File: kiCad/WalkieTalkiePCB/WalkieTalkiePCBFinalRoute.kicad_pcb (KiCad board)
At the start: 2 copper layers, 55 x 98 mm, 23 parts, among them SW1 UP, SW2 DWN, SW3 MODE, SW4 TLK, SW5 XTRA, U1 BAT-C-10TYPEC_(BMS), U2 PSM-301-Voltage-Regulator, U3 PBS-LED-1606WH-L_(Toggle_Butt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, U4 I2S-128X64-OLED-LCD_, U5 I2S-INMP441_(MIC), U6 Amplifier, U7 ESP-WROOM-32

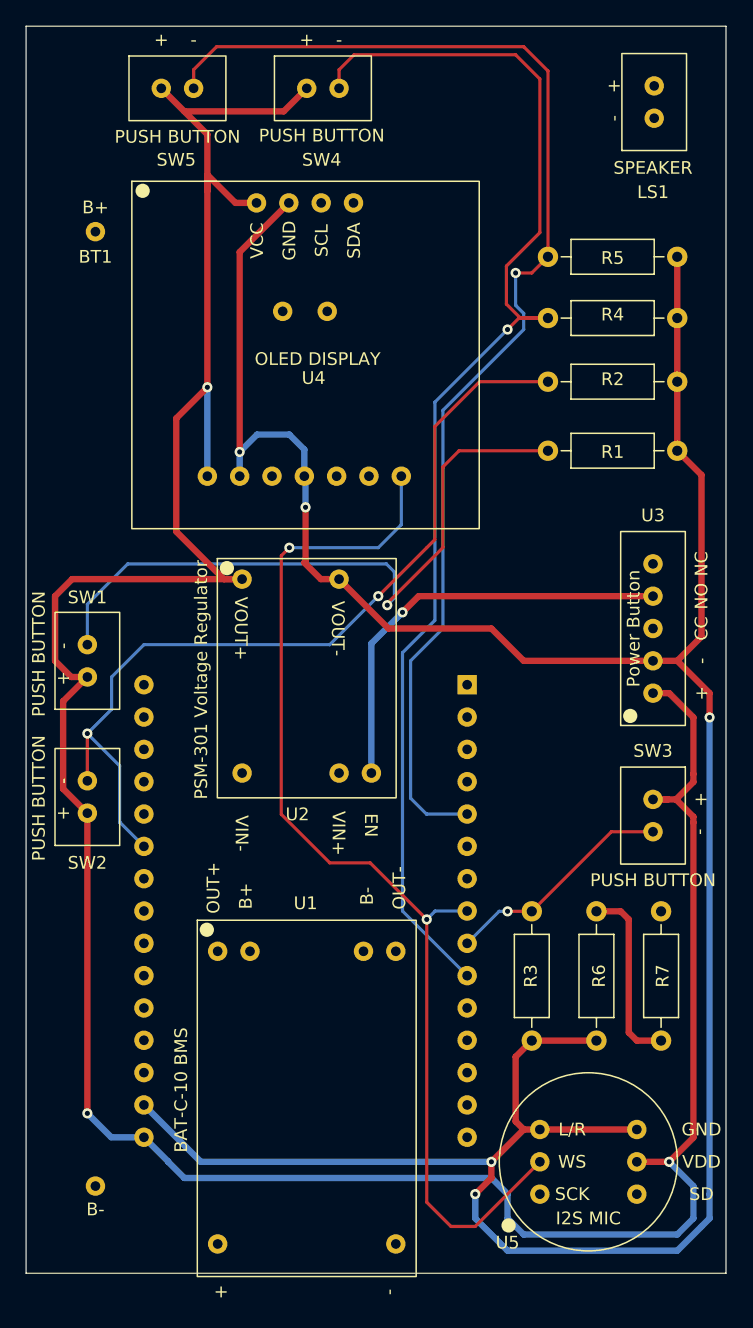
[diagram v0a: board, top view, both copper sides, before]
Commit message: Final Route of PCB
- Generated JLC gerber
- Created BOM
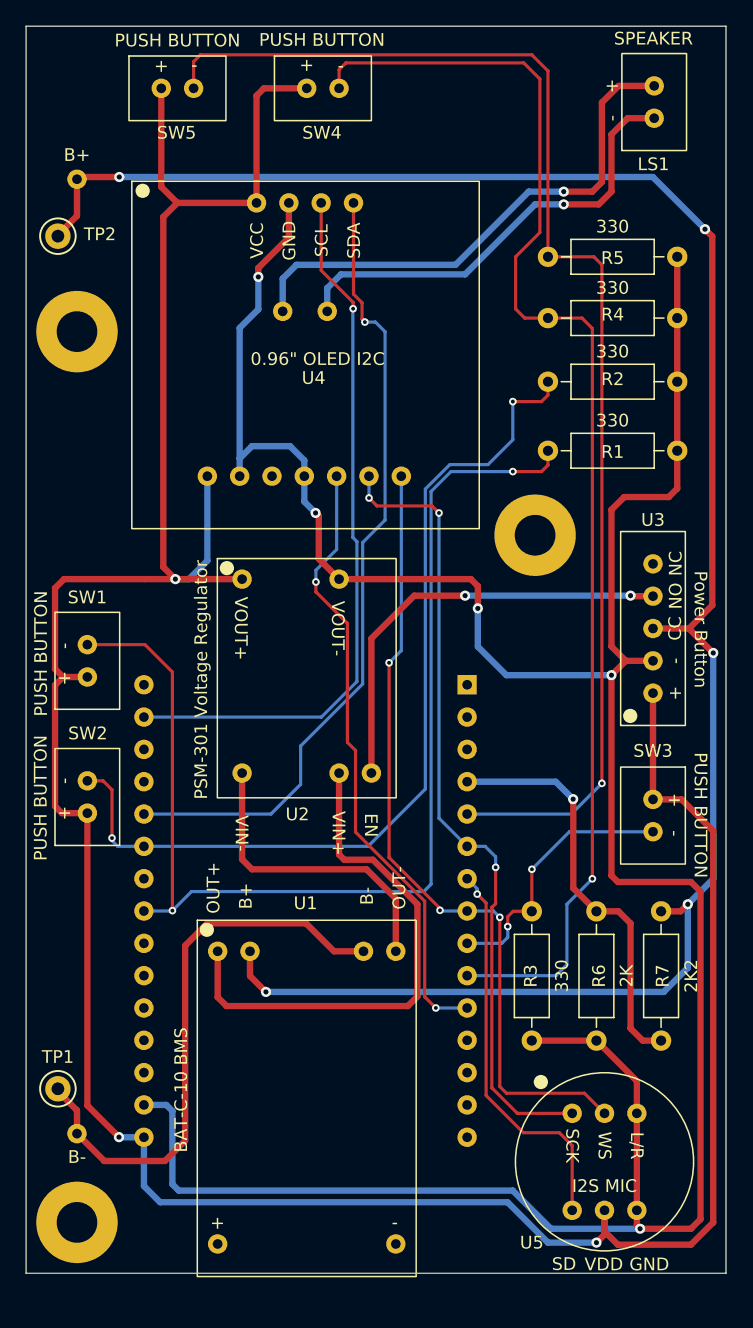
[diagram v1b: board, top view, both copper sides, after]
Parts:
- added REF**: MountingHole_3.2mm_M3_Pad, MountingHole:MountingHole_3.2mm_M3_Pad, F.Cu at (206.0, 93.0)
- added REF**: MountingHole_3.2mm_M3_Pad, MountingHole:MountingHole_3.2mm_M3_Pad, F.Cu at (170.0, 77.0)
- added REF**: MountingHole_3.2mm_M3_Pad, MountingHole:MountingHole_3.2mm_M3_Pad, F.Cu at (170.0, 147.0)
- added TP1: TestPoint_Keystone_5000-5004_Miniature, TestPoint:TestPoint_Keystone_5000-5004_Miniature, F.Cu at (168.5, 136.5)
- added TP2: TestPoint_Keystone_5000-5004_Miniature, TestPoint:TestPoint_Keystone_5000-5004_Miniature, F.Cu at (168.5, 69.5)
- BT1: value Battery_Cell -> 18650 Lithium Cell
- U2: value PSM-301-Voltage-Regulator -> PSM-301-Voltage-Regulator-3.3V
- U4: value I2S-128X64-OLED-LCD_ -> I2C-128X64-OLED-LCD
- U6: value Amplifier -> MAX98357A
- moved BT1 4.37 mm to (170.0, 65.0)
- moved U5 2.84 mm to (211.5, 141.0), turned to 0 degrees
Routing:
- net Net-(BT1-Pad1): track 0.00 -> 159.9 mm, vias 0 -> 5
- net Net-(U4-Pad4): track 0.00 -> 63.2 mm, vias 0 -> 1
- net Net-(U5-Pad1): track 0.00 -> 62.8 mm, vias 0 -> 3
- net Net-(U4-Pad3): track 0.00 -> 56.7 mm, vias 0 -> 1
- net Net-(U6-Pad3): track 0.00 -> 48.8 mm, vias 0 -> 2
- net Net-(BT1-Pad2): track 0.00 -> 45.3 mm
- net Net-(U6-Pad9): track 0.00 -> 41.7 mm, vias 0 -> 1
- net Net-(U1-Pad1): track 0.00 -> 41.3 mm
- net Net-(R1-Pad2): track 53.2 -> 91.8 mm, vias 1 -> 2
- net Net-(U6-Pad8): track 0.00 -> 35.7 mm, vias 0 -> 1
- net Net-(U5-Pad4): track 0.00 -> 31.1 mm, vias 0 -> 1
- net Net-(U1-Pad4): track 0.00 -> 24.3 mm
- net Net-(U5-Pad2): track 86.9 -> 63.5 mm, vias 2 -> 3
- net Net-(R6-Pad2): track 14.5 -> 32.6 mm, vias 0 -> 1
- net Net-(R5-Pad2): track 98.7 -> 102.1 mm
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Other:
- board text added: "JLCJLCJLCJLC"
- board text removed: "JLCJLCJLC"
